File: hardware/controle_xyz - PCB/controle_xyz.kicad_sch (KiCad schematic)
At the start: 14 parts, among them J1 Screw_Terminal_01x02, J10 Screw_Terminal_01x02, J11 Screw_Terminal_01x02, J12 Screw_Terminal_01x02, J2 Screw_Terminal_01x02, J3 Screw_Terminal_01x02, J4 Screw_Terminal_01x02, J5 Screw_Terminal_01x02, J6 Screw_Terminal_01x02, J7 Screw_Terminal_01x02, J9 Screw_Terminal_01x02, U1 logic_level_conversor

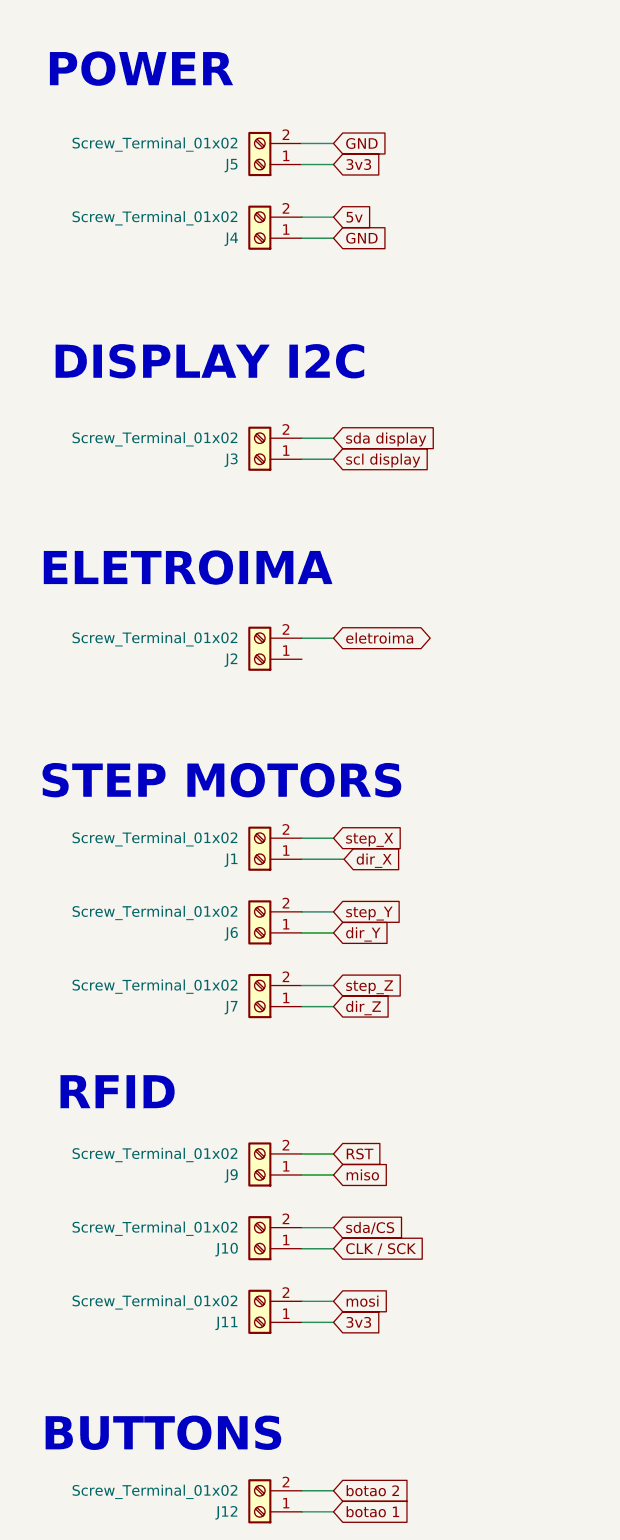
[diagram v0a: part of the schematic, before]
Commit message: Conectores de Borne Atualizados
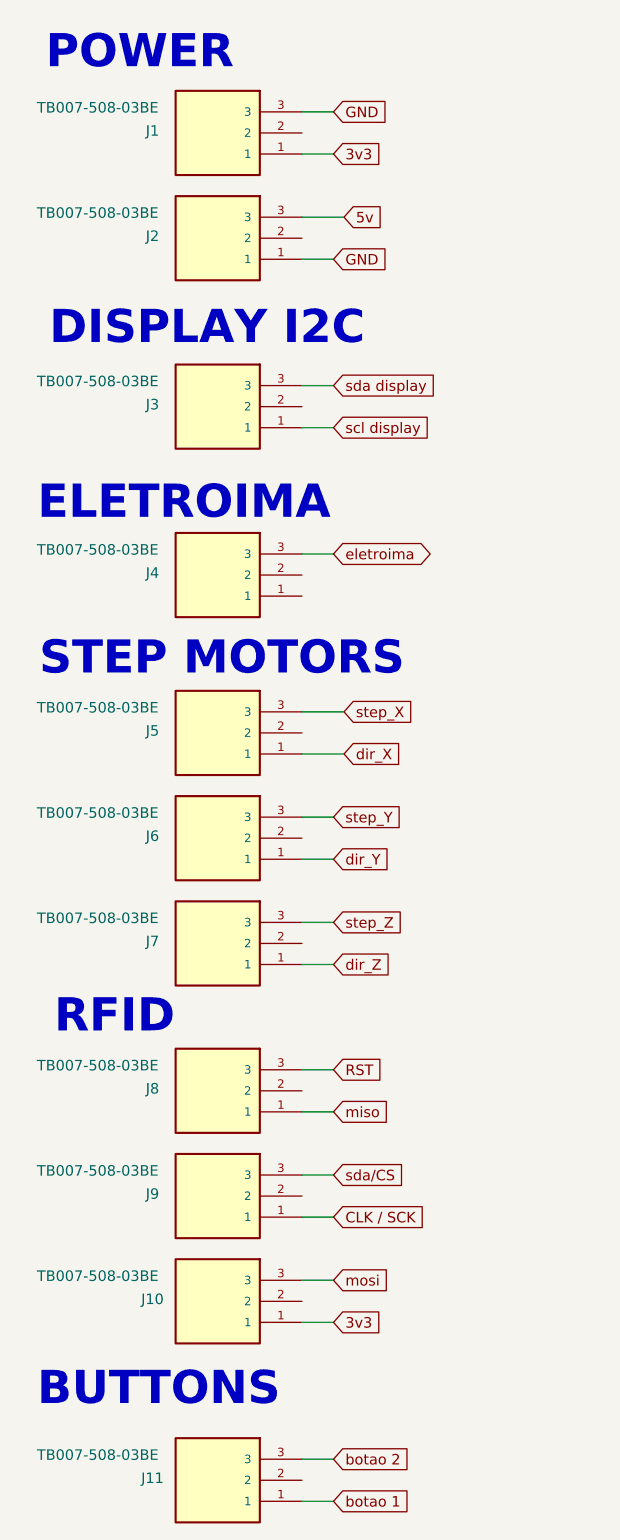
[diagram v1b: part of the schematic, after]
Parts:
- removed J1, J10, J11, J12, J2, J3, J4, J5, J6, J7, J9: Screw_Terminal_01x02, TerminalBlock_MetzConnect:TerminalBlock_MetzConnect_Type011_RT05502HBLC_1x02_P5.00mm_Horizontal, symbol Connector:Screw_Terminal_01x02
- added J1, J2, J3, J4, J5, J6, J7: TB007-508-03BE, CUI_TB007-508-03BE, symbol TB007-508-03BE:TB007-508-03BE
- added J10, J11, J8, J9: TB007-508-03BE, TerminalBlock_CUI:TerminalBlock_CUI_TB007-508-03_1x03_P5.08mm_Horizontal, symbol TB007-508-03BE:TB007-508-03BE
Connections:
- net 3v3: now also J1.1, J10.1
- net 5v: now also J2.3
- net CLK / SCK: now also J9.1
- net GND: now also J1.3, J2.1
- net RST: now also J8.3
- net botao 1: now also J11.1
- net botao 2: now also J11.3
- net dir_X: now also J5.1
- net dir_Y: now also J6.1
- net dir_Z: now also J7.1
- net eletroima: now also J4.3
- net miso: now also J8.1
- net mosi: now also J10.3
- net scl display: now also J3.1
- net sda display: now also J3.3
- net sda/CS: now also J9.3
- net step_X: now also J5.3
- net step_Y: now also J6.3
- net step_Z: now also J7.3

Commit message: update kicad prj
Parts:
- BZ1: footprint (none) -> Buzzer_Beeper:Buzzer_12x9.5RM7.6
- J1, J2, J3, J4, J5, J6, J7: footprint CUI_TB007-508-03BE -> TerminalBlock_CUI:TerminalBlock_CUI_TB007-508-03_1x03_P5.08mm_Horizontal
- U1: footprint (none) -> level_shifter:CONV_BOB-12009_level_shifter
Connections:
- no-connect marks 0 -> 12
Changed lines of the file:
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@@
 		(color 0 0 0 0)
 	)
+	(no_connect
+		(at 222.25 31.75)
+	)
+	(no_connect
+		(at 250.19 82.55)
+	)
+	(no_connect
+		(at 204.47 46.99)
+	)
+	(no_connect
+		(at 204.47 54.61)
+	)
+	(no_connect
+		(at 204.47 80.01)
+	)
+	(no_connect
+		(at 204.47 87.63)
+	)
+	(no_connect
+		(at 250.19 85.09)
+	)
+	(no_connect
+		(at 250.19 87.63)
+	)
+	(no_connect
+		(at 250.19 77.47)
+	)
+	(no_connect
+		(at 204.47 82.55)
+	)
+	(no_connect
+		(at 250.19 92.71)
+	)
+	(no_connect
+		(at 204.47 64.77)
+	)
 	(wire
 		(pts
@@
 			)
 		)
-		(property "Footprint" "CUI_TB007-508-03BE"
+		(property "Footprint" "TerminalBlock_CUI:TerminalBlock_CUI_TB007-508-03_1x03_P5.08mm_Horizontal"
 			(at 35.56 110.49 0)
 			(effects
@@
 			)
 		)
-		(property "Footprint" "CUI_TB007-508-03BE"
+		(property "Footprint" "TerminalBlock_CUI:TerminalBlock_CUI_TB007-508-03_1x03_P5.08mm_Horizontal"
 			(at 35.56 25.4 0)
 			(effects
@@
 			)
 		)
-		(property "Footprint" "CUI_TB007-508-03BE"
+		(property "Footprint" "TerminalBlock_CUI:TerminalBlock_CUI_TB007-508-03_1x03_P5.08mm_Horizontal"
 			(at 35.56 78.74 0)
 			(effects
@@
 			)
 		)
-		(property "Footprint" ""
+		(property "Footprint" "Buzzer_Beeper:Buzzer_12x9.5RM7.6"
 			(at 169.545 100.33 90)
 			(effects
@@
 			)
 		)
-		(property "Footprint" "CUI_TB007-508-03BE"
+		(property "Footprint" "TerminalBlock_CUI:TerminalBlock_CUI_TB007-508-03_1x03_P5.08mm_Horizontal"
 			(at 35.56 97.79 0)
 			(effects
@@
 			)
 		)
-		(property "Footprint" "CUI_TB007-508-03BE"
+		(property "Footprint" "TerminalBlock_CUI:TerminalBlock_CUI_TB007-508-03_1x03_P5.08mm_Horizontal"
 			(at 35.56 123.19 0)
 			(effects
@@
 			)
 		)
-		(property "Footprint" ""
+		(property "Footprint" "level_shifter:CONV_BOB-12009_level_shifter"
 			(at 90.424 71.374 0)
 			(effects
@@
 			)
 		)
-		(property "Footprint" "CUI_TB007-508-03BE"
+		(property "Footprint" "TerminalBlock_CUI:TerminalBlock_CUI_TB007-508-03_1x03_P5.08mm_Horizontal"
 			(at 35.56 38.1 0)
 			(effects
@@
 			)
 		)
-		(property "Footprint" "CUI_TB007-508-03BE"
+		(property "Footprint" "TerminalBlock_CUI:TerminalBlock_CUI_TB007-508-03_1x03_P5.08mm_Horizontal"
 			(at 35.56 58.42 0)
 			(effects
